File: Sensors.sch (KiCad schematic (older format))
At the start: 66 parts, among them U1 MPXH6250A, U6 SP720

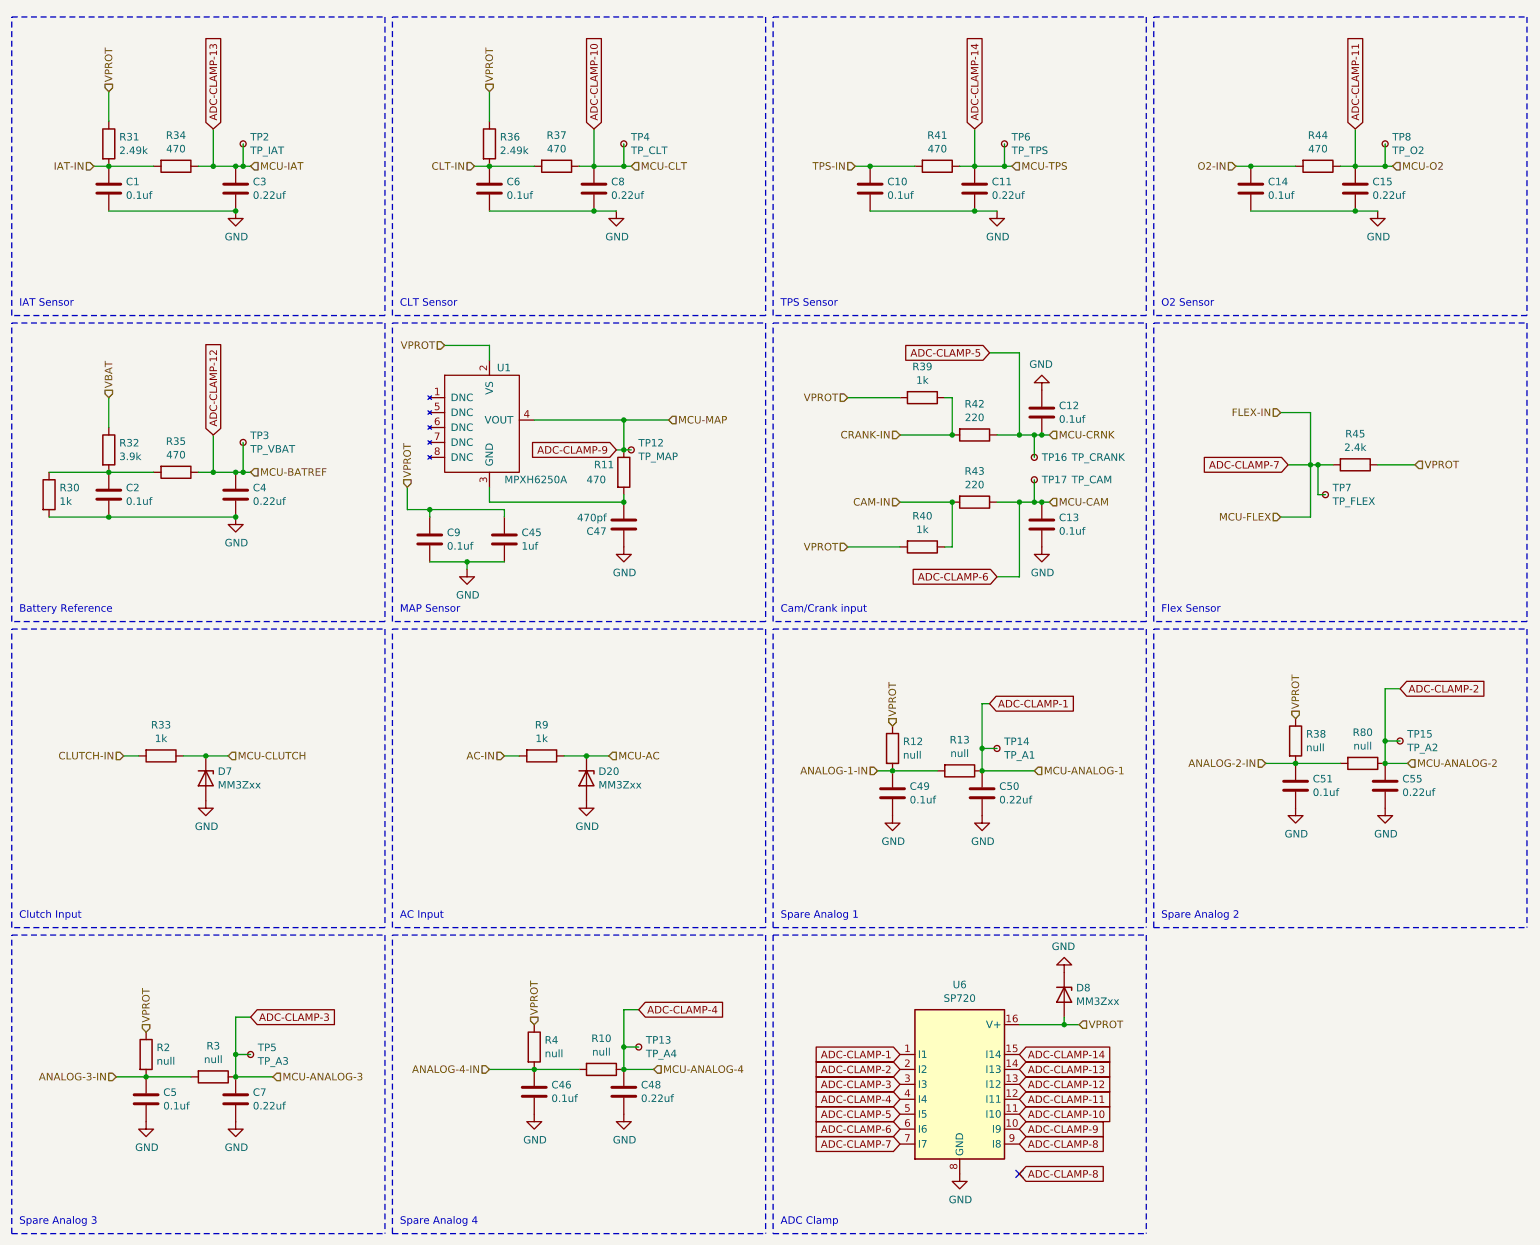
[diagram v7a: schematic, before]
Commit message: More routing updates
* added stitching vias
* organized sensor sheet
* moved the CAN and Security chips closer together to clean up fills
* added silkscreen text to some things
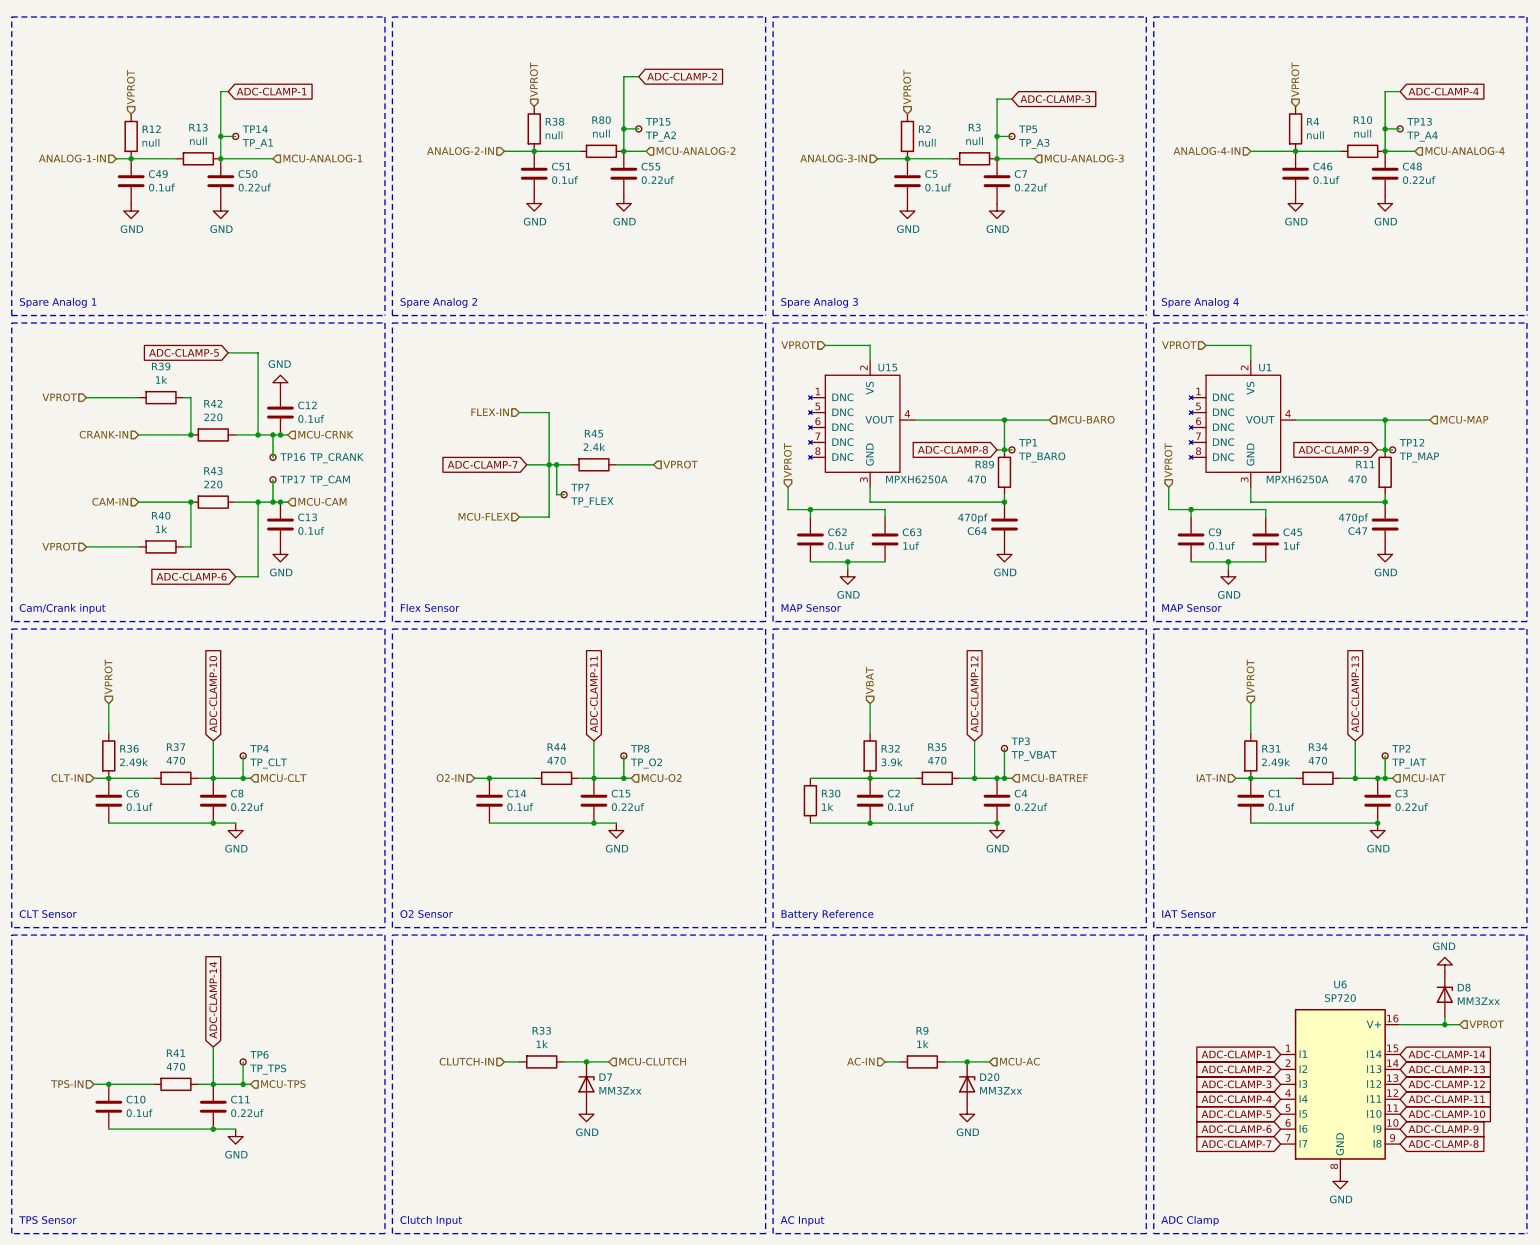
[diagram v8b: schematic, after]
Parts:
- added C62: 0.1uf, Capacitor_SMD:C_0805_2012Metric_Pad1.18x1.45mm_HandSolder, symbol Device:C
- added C63: 1uf, Capacitor_SMD:C_0805_2012Metric_Pad1.18x1.45mm_HandSolder, symbol Device:C
- added C64: 470pf, Capacitor_SMD:C_0805_2012Metric_Pad1.18x1.45mm_HandSolder, symbol Device:C
- added R89: 470, Resistor_SMD:R_0805_2012Metric_Pad1.20x1.40mm_HandSolder, symbol Device:R
- added TP1: TP_BARO, TestPoint:TestPoint_Pad_D1.0mm, symbol Connector:TestPoint_Small
- added U15: MPXH6250A, Sensor_Pressure:Freescale_98ARH99066A, symbol cone-kicad-parts:MPXH6250A
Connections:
- net ADC-CLAMP-8: now also R89.1, TP1.1, U15.4 (VOUT)
- net GND: now also C62.2, C63.2, C64.1
- net VPROT: now also C62.1, C63.1, U15.2 (VS)
- new net: C64.2, R89.2, U15.3 (GND)
- no-connect marks 1 -> 0
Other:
- moved on the sheet: C1, C10, C11, C12, C13, C14, C15, C2, C3, C4, C45, C46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
